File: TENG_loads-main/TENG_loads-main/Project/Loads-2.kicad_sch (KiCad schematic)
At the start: 24 parts, among them K17 V23079C1103B301, K18 V23079C1103B301, K19 V23079C1103B301, K20 V23079C1103B301, K21 V23079C1103B301, K22 IMC03TS, K23 IMC03TS, K24 IMC03TS, K25 IMC03TS, K26 IMC03TS, K27 V23079C1103B301, K28 V23079C1103B301, K29 V23079C1103B301, K30 IMC03TS, K31 IMC03TS, K32 IMC03TS

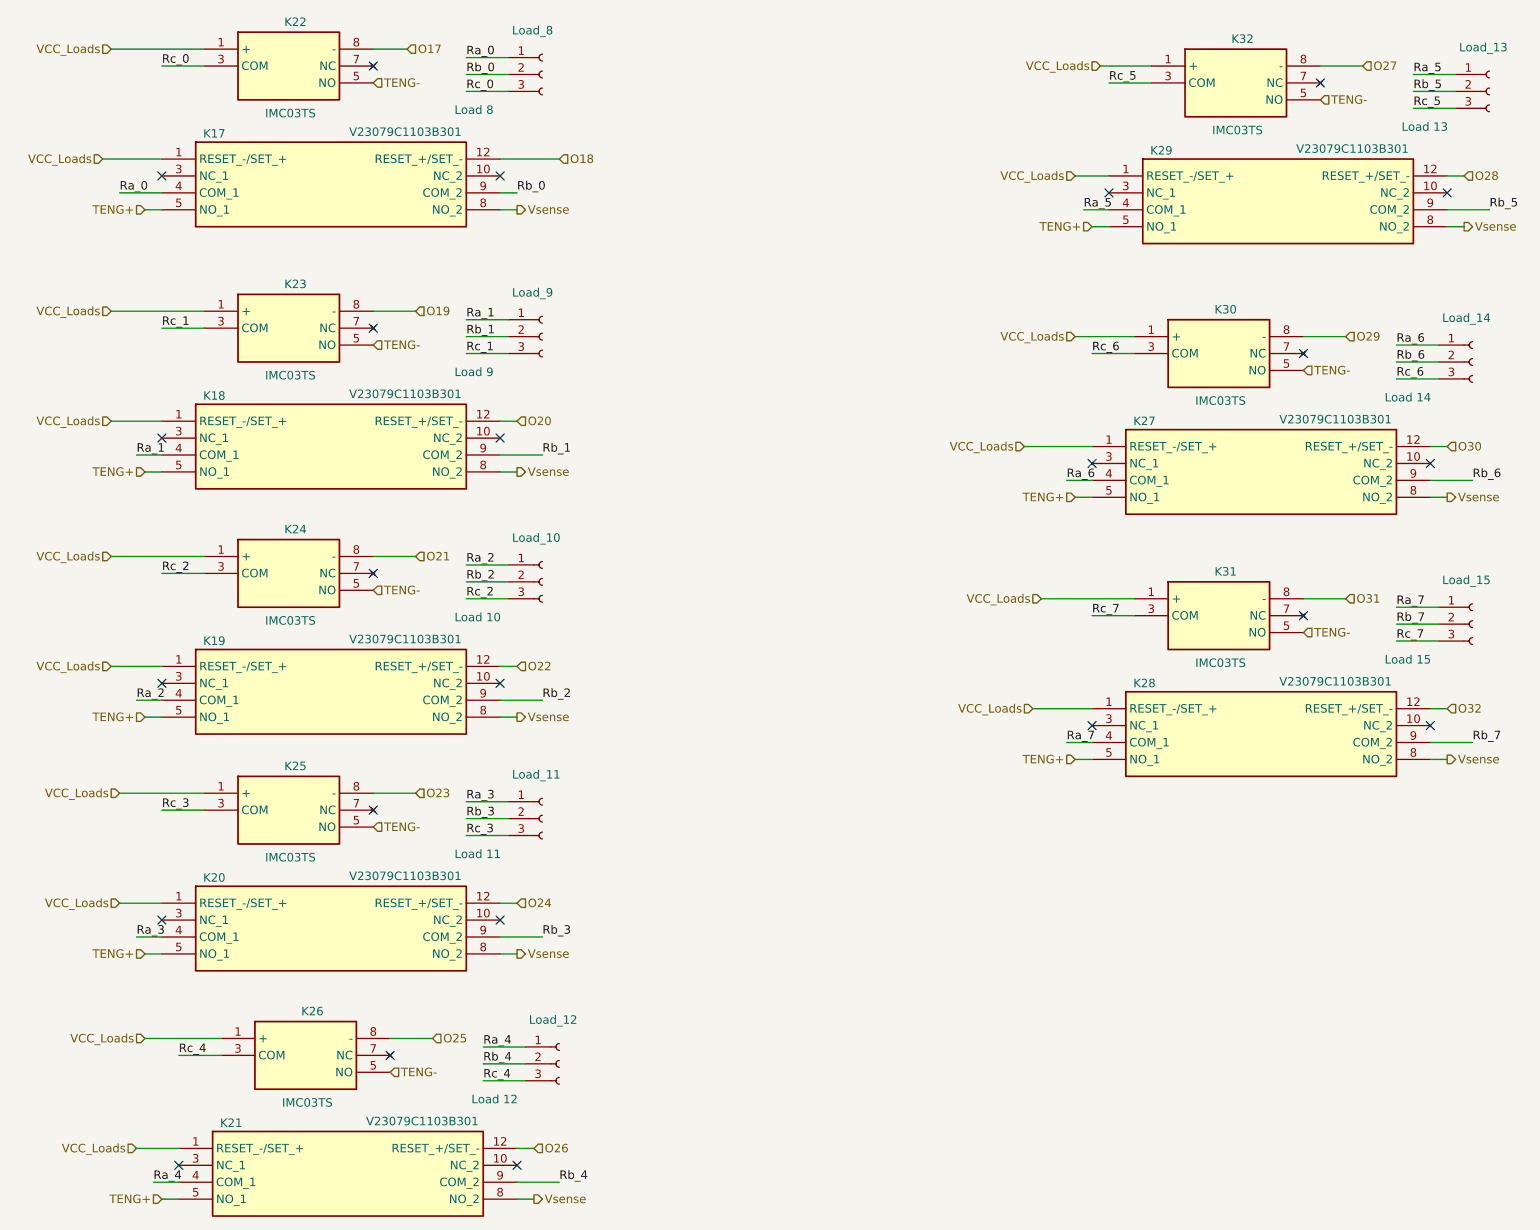
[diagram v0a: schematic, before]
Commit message: Changed Relay identifier
Changed relay identifier with the correct one (12 VDC changed to 5 VDC).
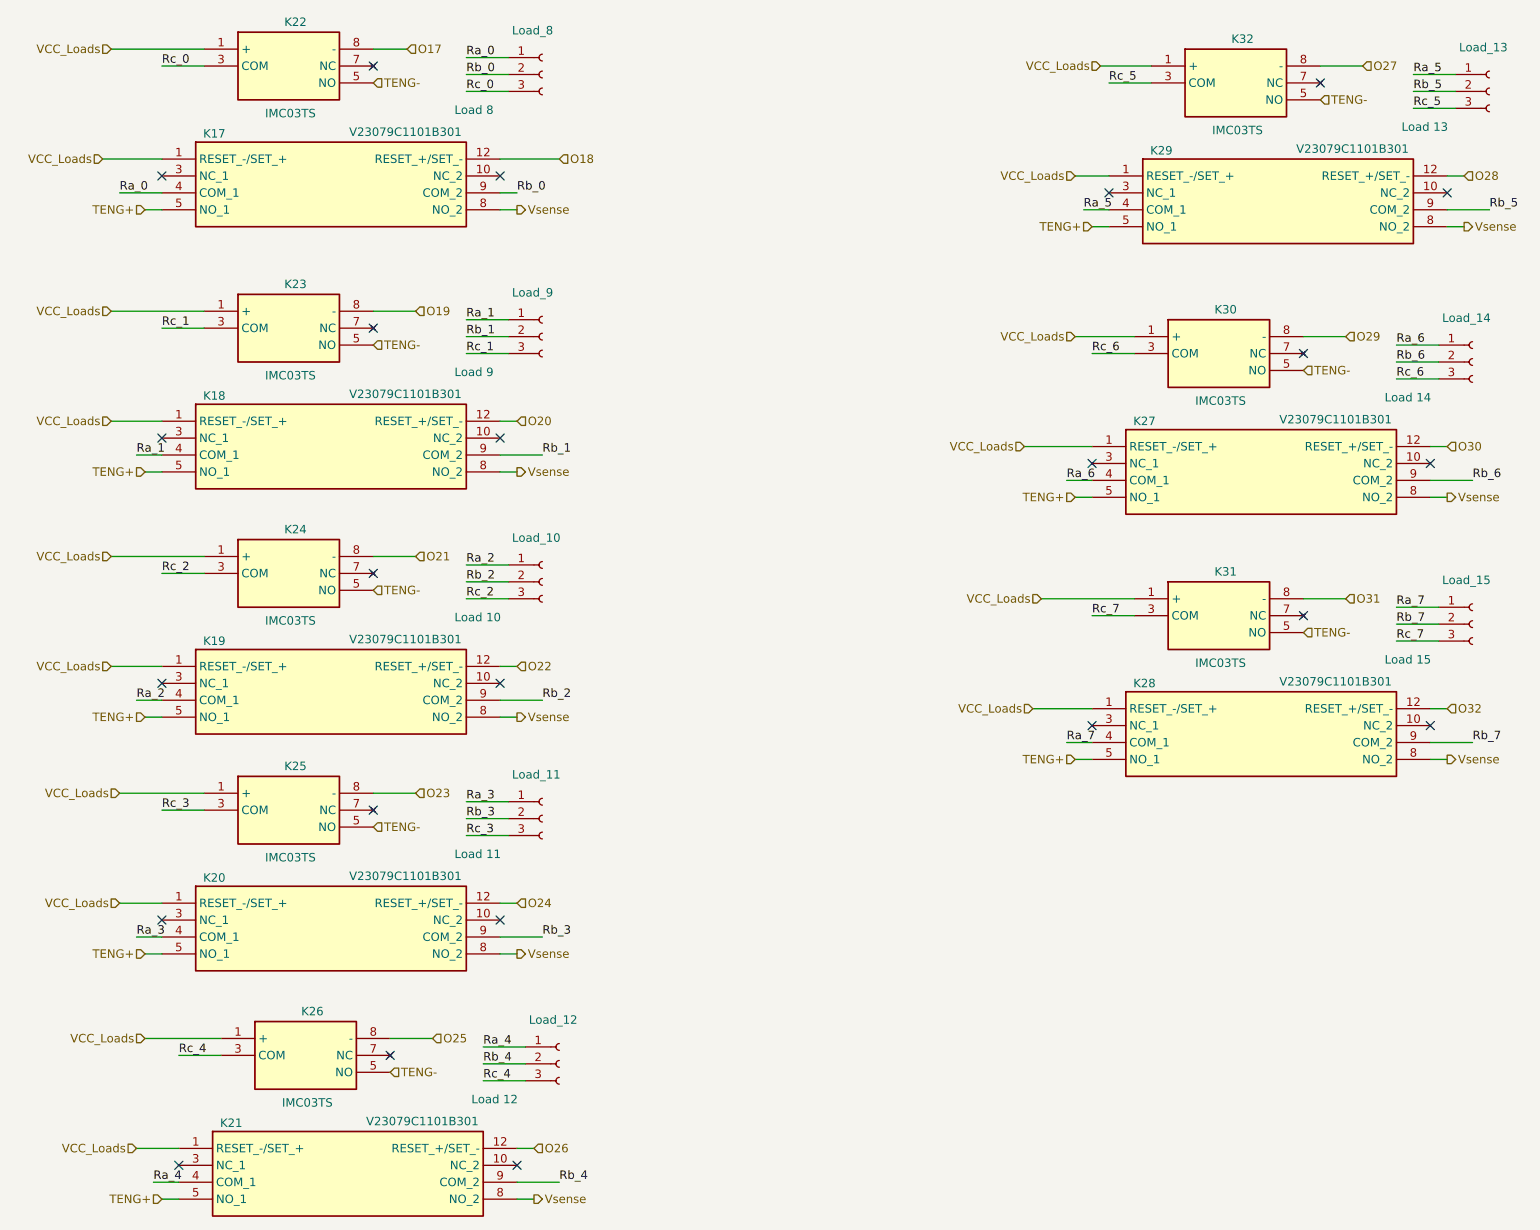
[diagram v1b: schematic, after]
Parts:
- K17, K18, K19, K20, K21, K27, K28, K29: value V23079C1103B301 -> V23079C1101B301
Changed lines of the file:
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@@
 			)
 		)
-		(property "Value" "V23079C1103B301"
+		(property "Value" "V23079C1101B301"
 			(at 105.156 72.136 0)
 			(effects
@@
 			)
 		)
-		(property "Value" "V23079C1103B301"
+		(property "Value" "V23079C1101B301"
 			(at 107.696 181.356 0)
 			(effects
@@
 			)
 		)
-		(property "Value" "V23079C1103B301"
+		(property "Value" "V23079C1101B301"
 			(at 244.856 115.316 0)
 			(effects
@@
 			)
 		)
-		(property "Value" "V23079C1103B301"
+		(property "Value" "V23079C1101B301"
 			(at 105.156 144.526 0)
 			(effects
@@
 			)
 		)
-		(property "Value" "V23079C1103B301"
+		(property "Value" "V23079C1101B301"
 			(at 247.396 35.306 0)
 			(effects
@@
 			)
 		)
-		(property "Value" "V23079C1103B301"
+		(property "Value" "V23079C1101B301"
 			(at 244.856 75.946 0)
 			(effects
@@
 			)
 		)
-		(property "Value" "V23079C1103B301"
+		(property "Value" "V23079C1101B301"
 			(at 105.156 108.966 0)
 			(effects
@@
 			)
 		)
-		(property "Value" "V23079C1103B301"
+		(property "Value" "V23079C1101B301"
 			(at 105.156 32.766 0)
 			(effects

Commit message: Capacitor and relay changes
Capacitor correction and relay ID correction
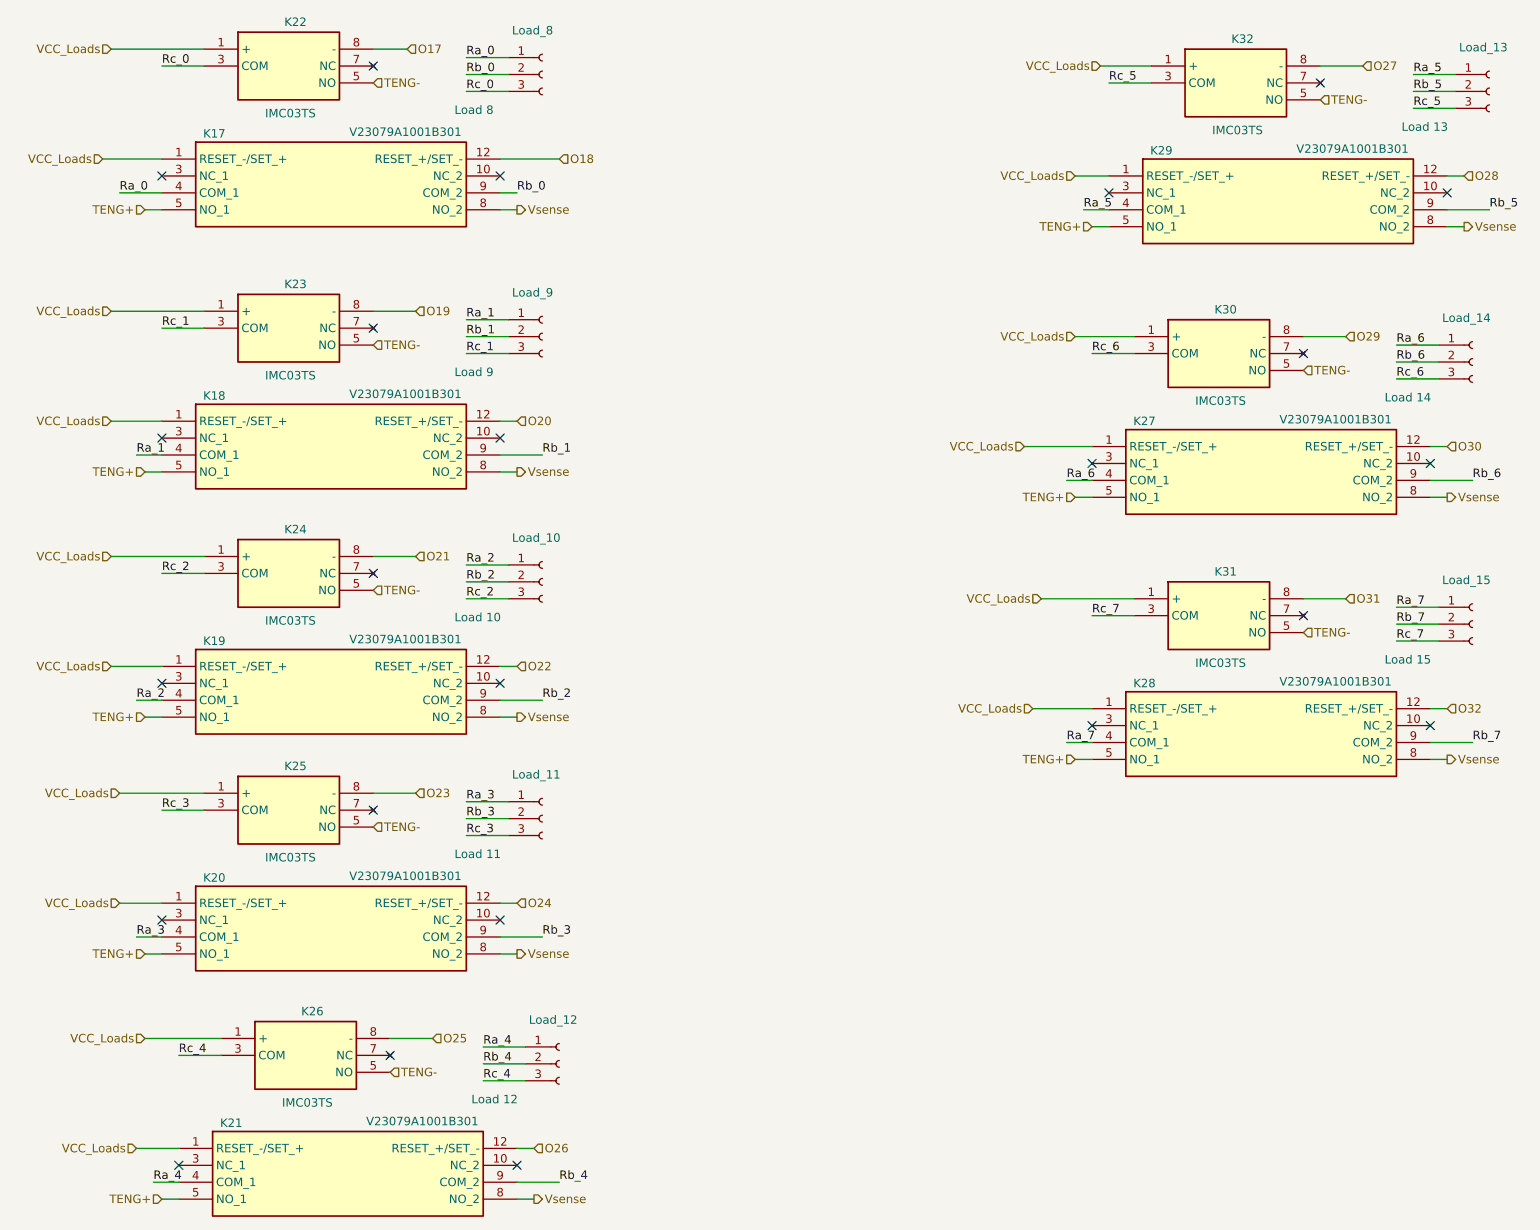
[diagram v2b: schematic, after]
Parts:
- K17, K18, K19, K20, K21, K27, K28, K29: value V23079C1101B301 -> V23079A1001B301
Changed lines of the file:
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@@
 			)
 		)
-		(property "Value" "V23079C1101B301"
+		(property "Value" "V23079A1001B301"
 			(at 105.156 72.136 0)
 			(effects
@@
 			)
 		)
-		(property "Value" "V23079C1101B301"
+		(property "Value" "V23079A1001B301"
 			(at 107.696 181.356 0)
 			(effects
@@
 			)
 		)
-		(property "Value" "V23079C1101B301"
+		(property "Value" "V23079A1001B301"
 			(at 244.856 115.316 0)
 			(effects
@@
 			)
 		)
-		(property "Value" "V23079C1101B301"
+		(property "Value" "V23079A1001B301"
 			(at 105.156 144.526 0)
 			(effects
@@
 			)
 		)
-		(property "Value" "V23079C1101B301"
+		(property "Value" "V23079A1001B301"
 			(at 247.396 35.306 0)
 			(effects
@@
 			)
 		)
-		(property "Value" "V23079C1101B301"
+		(property "Value" "V23079A1001B301"
 			(at 244.856 75.946 0)
 			(effects
@@
 			)
 		)
-		(property "Value" "V23079C1101B301"
+		(property "Value" "V23079A1001B301"
 			(at 105.156 108.966 0)
 			(effects
@@
 			)
 		)
-		(property "Value" "V23079C1101B301"
+		(property "Value" "V23079A1001B301"
 			(at 105.156 32.766 0)
 			(effects
